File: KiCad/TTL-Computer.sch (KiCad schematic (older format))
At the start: 0 parts

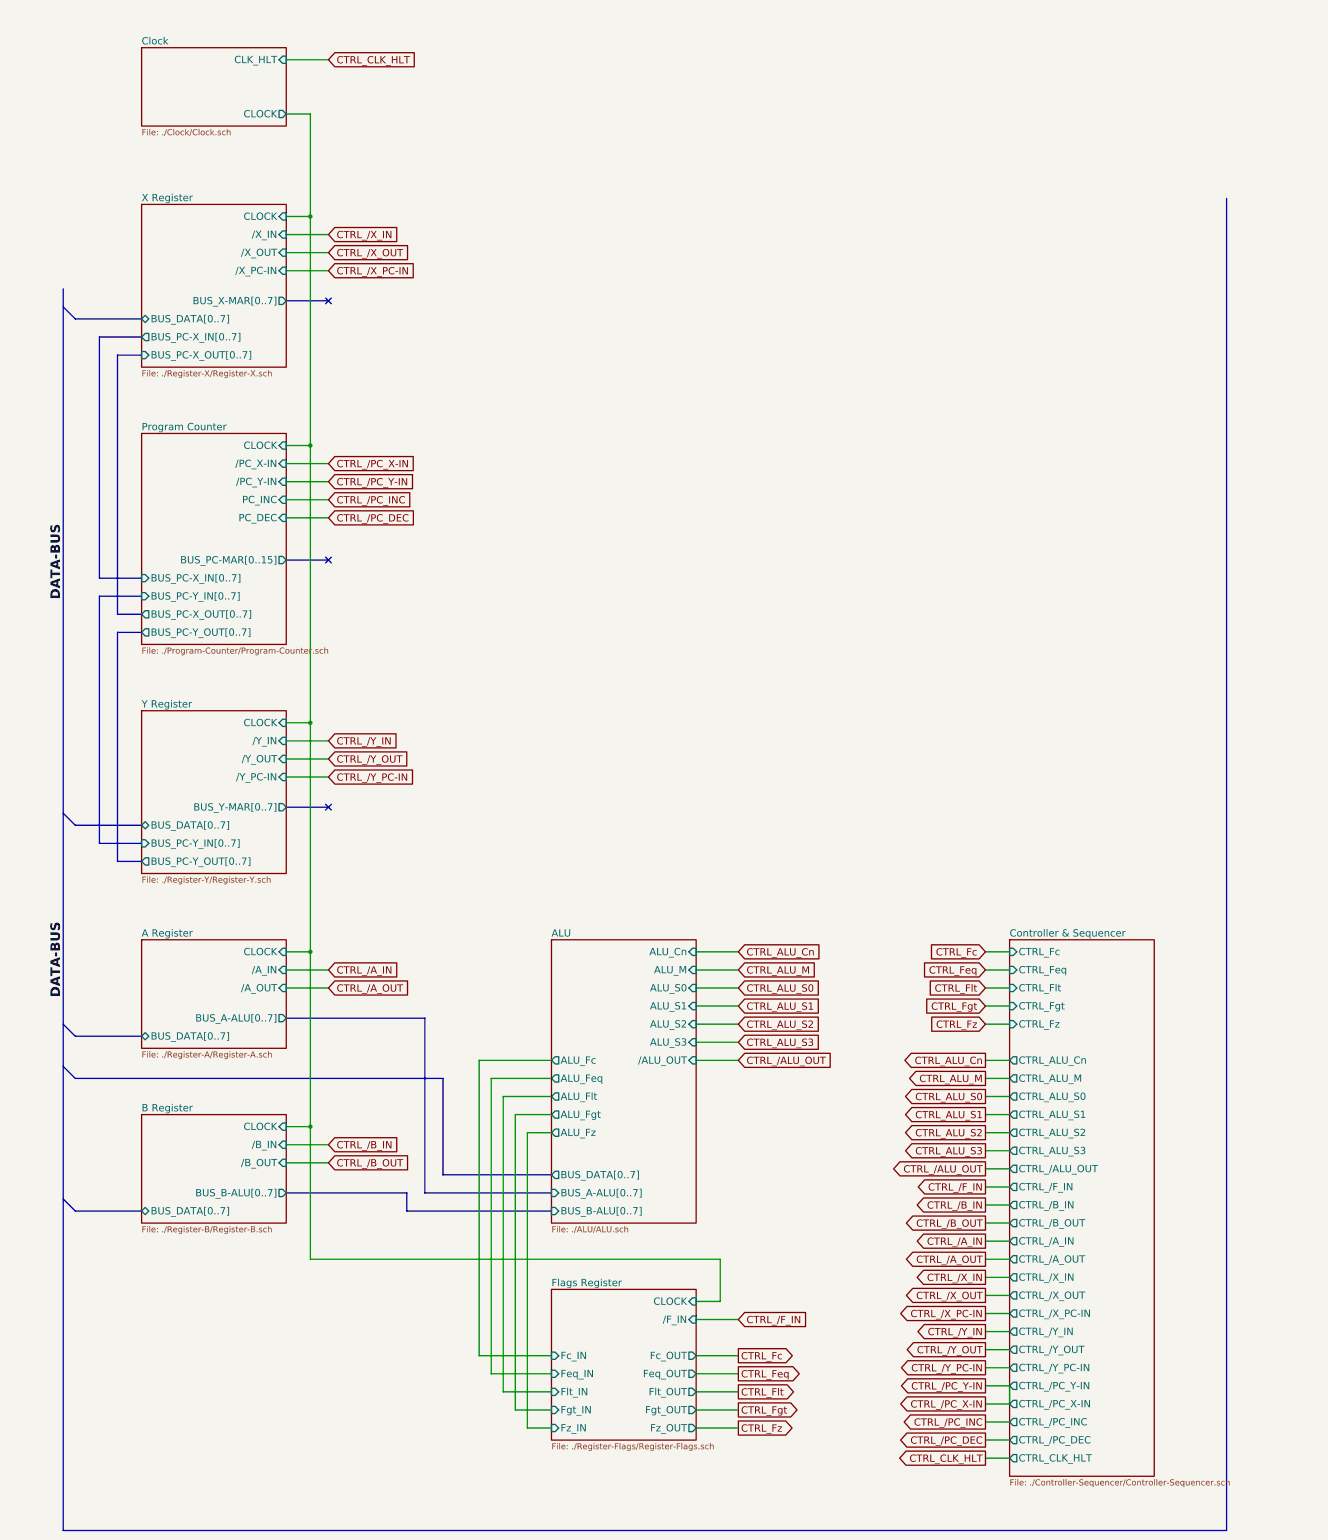
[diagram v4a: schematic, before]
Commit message: Improved ALU and instructions (ALU now takes data from all registers)
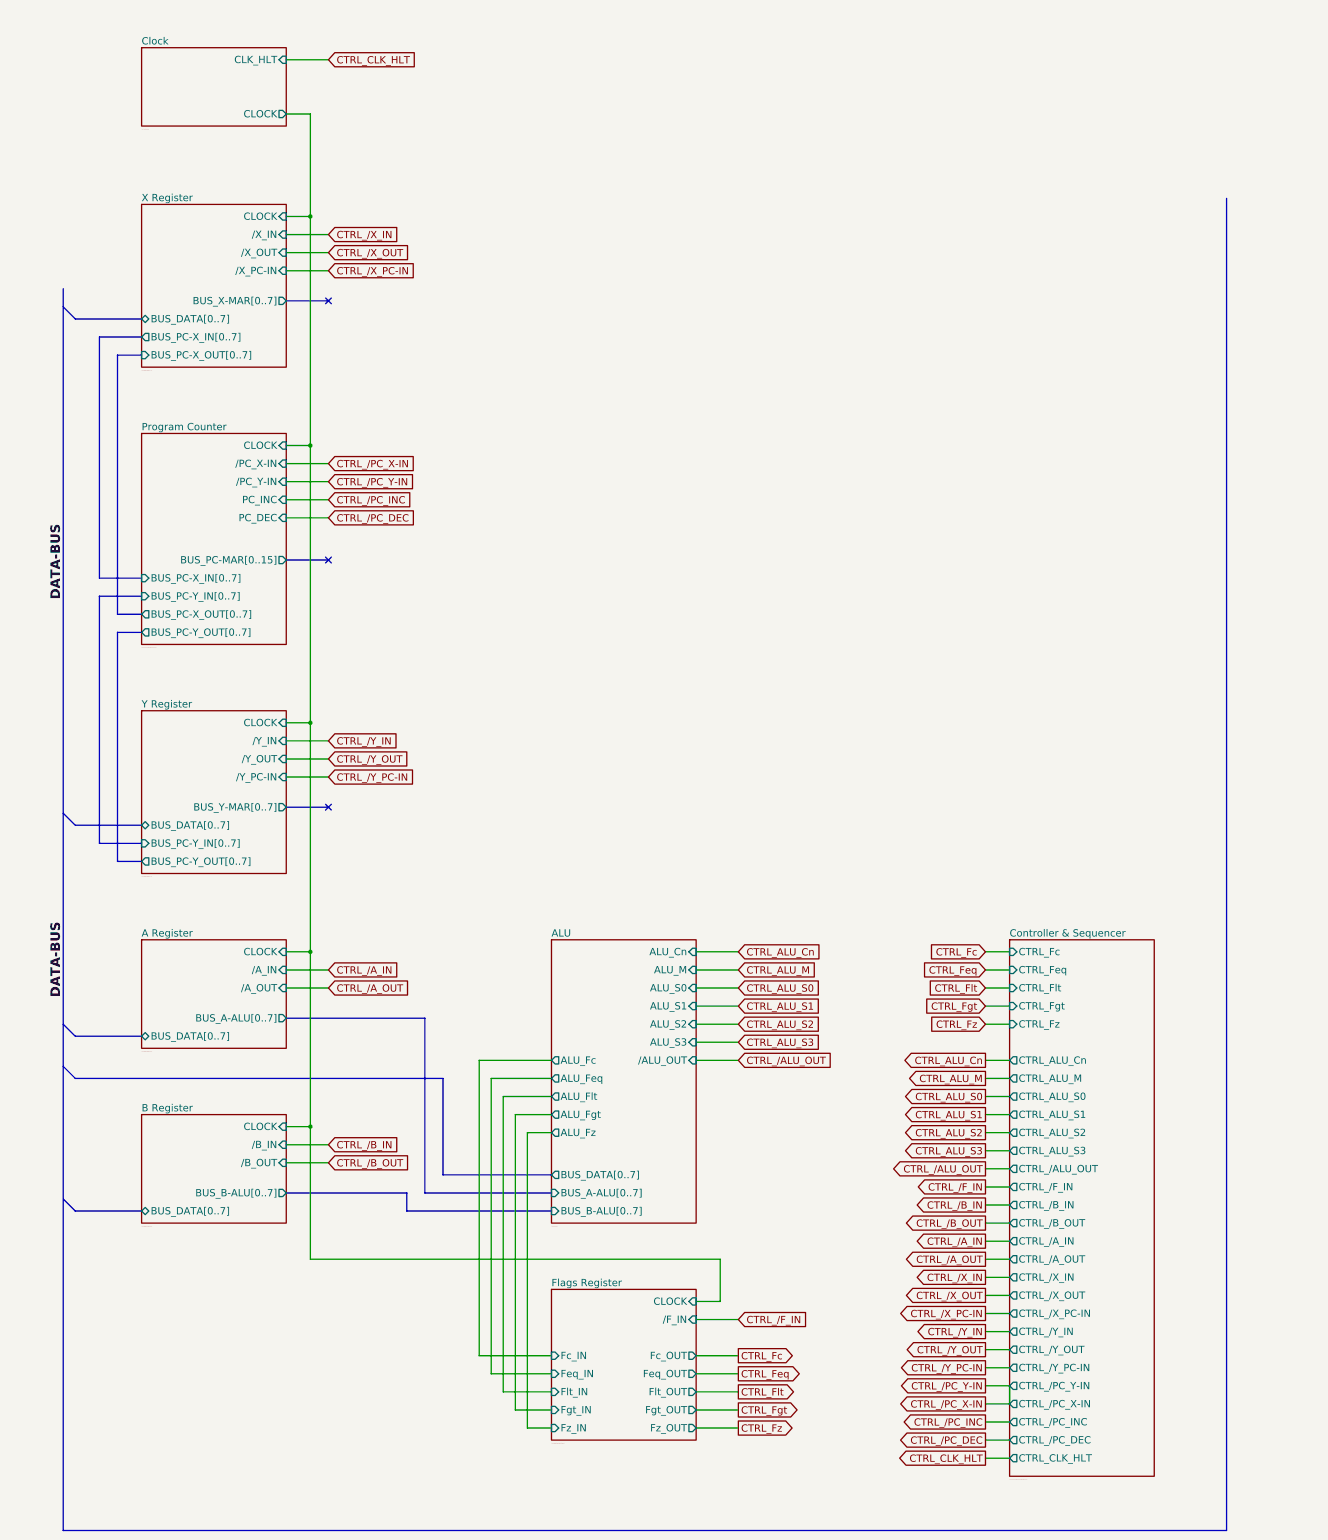
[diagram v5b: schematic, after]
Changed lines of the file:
@@
 U 5ACF3206
 F0 "Clock" 60
-F1 "./Clock/Clock.sch" 0
+F1 "./Clock/Clock.sch" 4
 F2 "CLOCK" O R 2850 1550 60
 F3 "CLK_HLT" I R 2850 1100 60
@@
 U 5ACF2F0F
 F0 "X Register" 60
-F1 "./Register-X/Register-X.sch" 0
+F1 "./Register-X/Register-X.sch" 4
 F2 "CLOCK" I R 2850 2400 60
 F3 "/X_IN" I R 2850 2550 60
@@
 U 5AD0848F
 F0 "Y Register" 60
-F1 "./Register-Y/Register-Y.sch" 0
+F1 "./Register-Y/Register-Y.sch" 4
 F2 "BUS_PC-Y_IN[0..7]" I L 1650 7600 60
 F3 "BUS_DATA[0..7]" B L 1650 7450 60
@@
 U 5ACF340E
 F0 "Program Counter" 60
-F1 "./Program-Counter/Program-Counter.sch" 0
+F1 "./Program-Counter/Program-Counter.sch" 4
 F2 "/PC_X-IN" I R 2850 4450 60
 F3 "/PC_Y-IN" I R 2850 4600 60
@@
 U 5AD5CFF9
 F0 "ALU" 60
-F1 "./ALU/ALU.sch" 0
+F1 "./ALU/ALU.sch" 4
 F2 "ALU_Cn" I R 6250 8500 60
 F3 "ALU_M" I R 6250 8650 60
@@
 U 5AEB52B5
 F0 "B Register" 60
-F1 "./Register-B/Register-B.sch" 0
+F1 "./Register-B/Register-B.sch" 4
 F2 "/B_OUT" I R 2850 10250 60
 F3 "CLOCK" I R 2850 9950 60
@@
 U 5AEB1288
 F0 "A Register" 60
-F1 "./Register-A/Register-A.sch" 0
+F1 "./Register-A/Register-A.sch" 4
 F2 "/A_OUT" I R 2850 8800 60
 F3 "CLOCK" I R 2850 8500 60
@@
 U 5AECAFE0
 F0 "Flags Register" 60
-F1 "./Register-Flags/Register-Flags.sch" 0
+F1 "./Register-Flags/Register-Flags.sch" 4
 F2 "CLOCK" I R 6250 11400 60
 F3 "/F_IN" I R 6250 11550 60
@@
 U 5AF221CC
 F0 "Controller & Sequencer" 60
-F1 "./Controller-Sequencer/Controller-Sequencer.sch" 0
+F1 "./Controller-Sequencer/Controller-Sequencer.sch" 4
 F2 "CTRL_Fc" I L 8850 8500 60
 F3 "CTRL_Feq" I L 8850 8650 60

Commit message: Renamed registers X and Y to C and D.
ALU now has its own internal accumulator register.
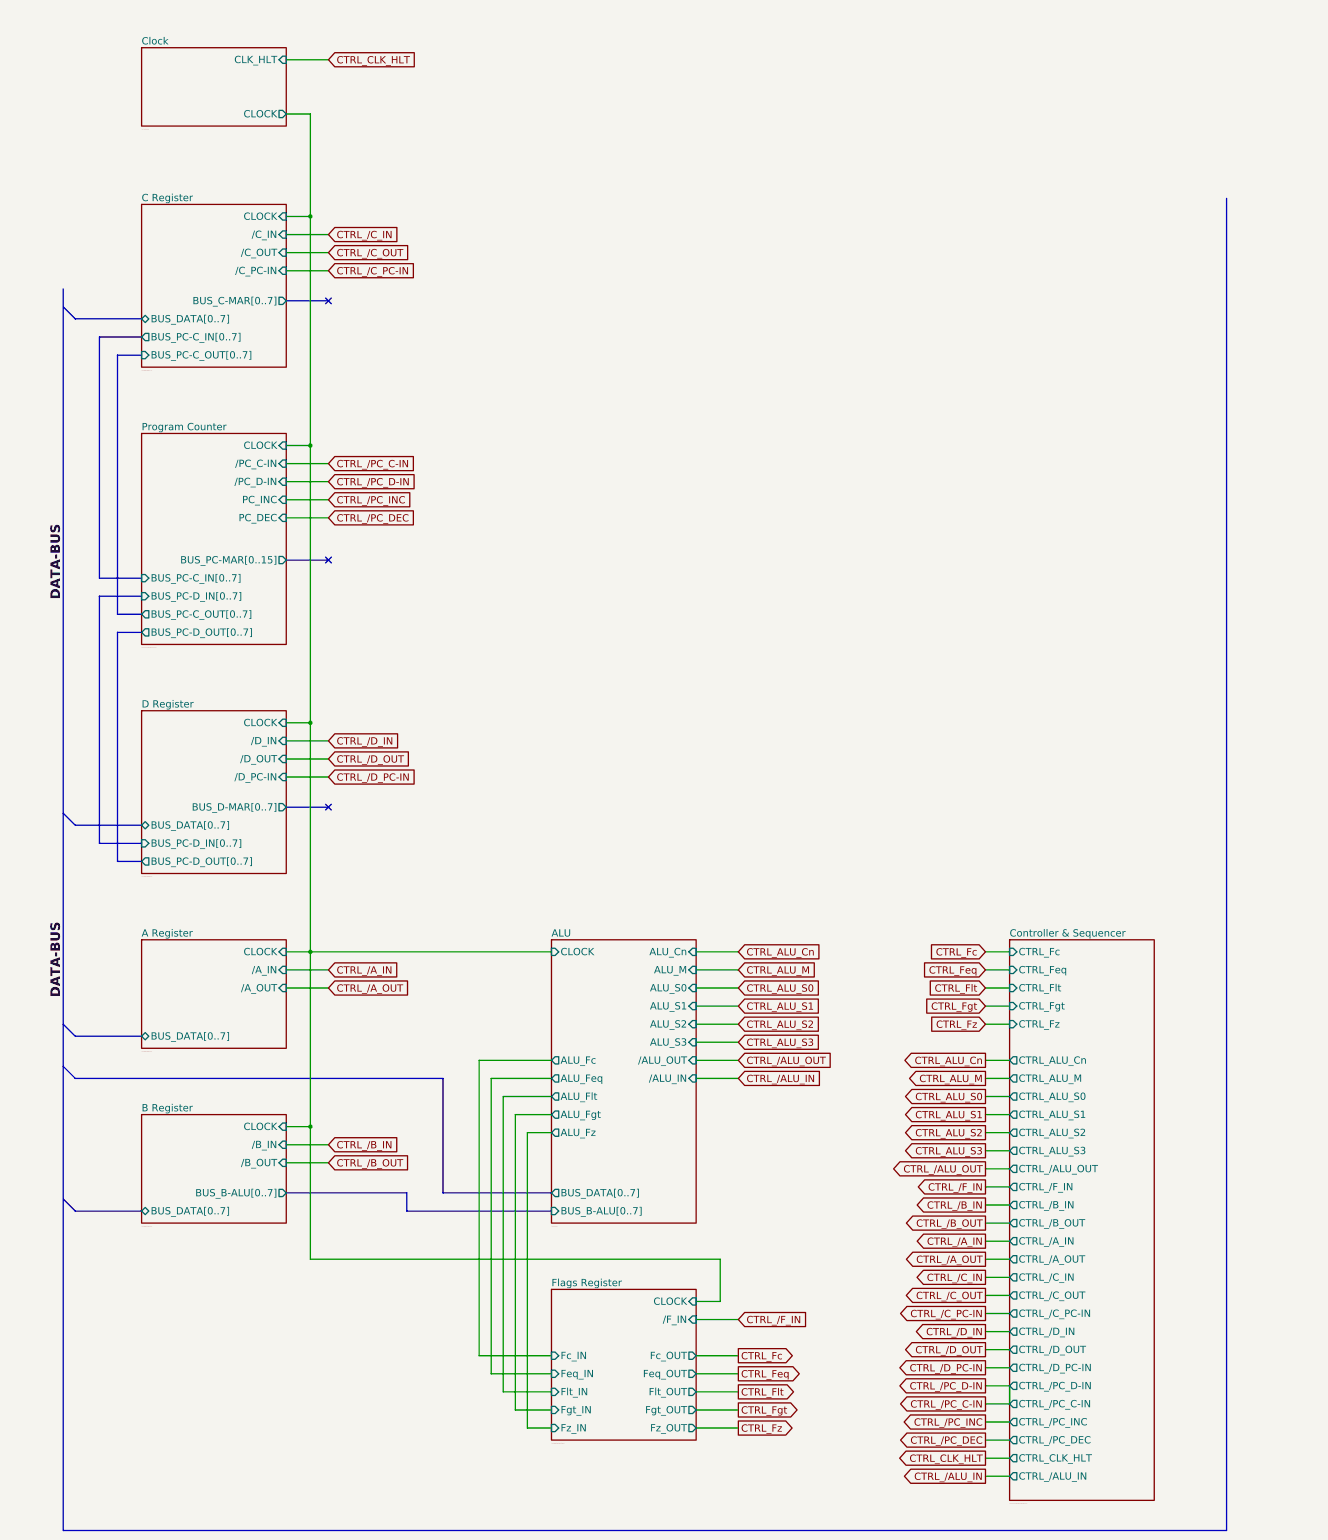
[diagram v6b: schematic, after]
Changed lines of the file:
@@
 S 1650 2300 1200 1350
 U 5ACF2F0F
-F0 "X Register" 60
-F1 "./Register-X/Register-X.sch" 4
+F0 "C Register" 60
+F1 "./Register-C/Register-C.sch" 4
 F2 "CLOCK" I R 2850 2400 60
-F3 "/X_IN" I R 2850 2550 60
-F4 "/X_OUT" I R 2850 2700 60
-F5 "/X_PC-IN" I R 2850 2850 60
+F3 "/C_IN" I R 2850 2550 60
+F4 "/C_OUT" I R 2850 2700 60
+F5 "/C_PC-IN" I R 2850 2850 60
 F6 "BUS_DATA[0..7]" B L 1650 3250 60
-F7 "BUS_PC-X_OUT[0..7]" I L 1650 3550 60
-F8 "BUS_X-MAR[0..7]" O R 2850 3100 60
-F9 "BUS_PC-X_IN[0..7]" O L 1650 3400 60
+F7 "BUS_PC-C_OUT[0..7]" I L 1650 3550 60
+F8 "BUS_C-MAR[0..7]" O R 2850 3100 60
+F9 "BUS_PC-C_IN[0..7]" O L 1650 3400 60
 $EndSheet
 $Sheet
 S 1650 6500 1200 1350
 U 5AD0848F
-F0 "Y Register" 60
-F1 "./Register-Y/Register-Y.sch" 4
-F2 "BUS_PC-Y_IN[0..7]" I L 1650 7600 60
+F0 "D Register" 60
+F1 "./Register-D/Register-D.sch" 4
+F2 "BUS_PC-D_IN[0..7]" I L 1650 7600 60
 F3 "BUS_DATA[0..7]" B L 1650 7450 60
 F4 "CLOCK" I R 2850 6600 60
-F5 "BUS_Y-MAR[0..7]" O R 2850 7300 60
-F6 "/Y_IN" I R 2850 6750 60
-F7 "/Y_OUT" I R 2850 6900 60
-F8 "/Y_PC-IN" I R 2850 7050 60
-F9 "BUS_PC-Y_OUT[0..7]" O L 1650 7750 60
+F5 "BUS_D-MAR[0..7]" O R 2850 7300 60
+F6 "/D_IN" I R 2850 6750 60
+F7 "/D_OUT" I R 2850 6900 60
+F8 "/D_PC-IN" I R 2850 7050 60
+F9 "BUS_PC-D_OUT[0..7]" O L 1650 7750 60
 $EndSheet
 $Sheet
@@
 F0 "Program Counter" 60
 F1 "./Program-Counter/Program-Counter.sch" 4
-F2 "/PC_X-IN" I R 2850 4450 60
-F3 "/PC_Y-IN" I R 2850 4600 60
+F2 "/PC_C-IN" I R 2850 4450 60
+F3 "/PC_D-IN" I R 2850 4600 60
 F4 "PC_INC" I R 2850 4750 60
 F5 "PC_DEC" I R 2850 4900 60
 F6 "CLOCK" I R 2850 4300 60
-F7 "BUS_PC-X_OUT[0..7]" O L 1650 5700 60
-F8 "BUS_PC-Y_OUT[0..7]" O L 1650 5850 60
+F7 "BUS_PC-C_OUT[0..7]" O L 1650 5700 60
+F8 "BUS_PC-D_OUT[0..7]" O L 1650 5850 60
 F9 "BUS_PC-MAR[0..15]" O R 2850 5250 60
-F10 "BUS_PC-X_IN[0..7]" I L 1650 5400 60
-F11 "BUS_PC-Y_IN[0..7]" I L 1650 5550 60
+F10 "BUS_PC-C_IN[0..7]" I L 1650 5400 60
+F11 "BUS_PC-D_IN[0..7]" I L 1650 5550 60
 $EndSheet
 $Sheet
@@
 F2 "ALU_Cn" I R 6250 8500 60
 F3 "ALU_M" I R 6250 8650 60
-F4 "BUS_A-ALU[0..7]" I L 5050 10500 60
-F5 "BUS_B-ALU[0..7]" I L 5050 10650 60
-F6 "ALU_S0" I R 6250 8800 60
-F7 "ALU_S1" I R 6250 8950 60
-F8 "ALU_S2" I R 6250 9100 60
-F9 "ALU_S3" I R 6250 9250 60
-F10 "ALU_Feq" O L 5050 9550 60
-F11 "ALU_Flt" O L 5050 9700 60
-F12 "ALU_Fgt" O L 5050 9850 60
-F13 "/ALU_OUT" I R 6250 9400 60
-F14 "BUS_DATA[0..7]" O L 5050 10350 60
-F15 "ALU_Fz" O L 5050 10000 60
-F16 "ALU_Fc" O L 5050 9400 60
+F4 "BUS_B-ALU[0..7]" I L 5050 10650 60
+F5 "ALU_S0" I R 6250 8800 60
+F6 "ALU_S1" I R 6250 8950 60
+F7 "ALU_S2" I R 6250 9100 60
+F8 "ALU_S3" I R 6250 9250 60
+F9 "ALU_Feq" O L 5050 9550 60
+F10 "ALU_Flt" O L 5050 9700 60
+F11 "ALU_Fgt" O L 5050 9850 60
+F12 "/ALU_OUT" I R 6250 9400 60
+F13 "BUS_DATA[0..7]" O L 5050 10500 60
+F14 "ALU_Fz" O L 5050 10000 60
+F15 "ALU_Fc" O L 5050 9400 60
+F16 "CLOCK" I L 5050 8500 60
+F17 "/ALU_IN" I R 6250 9550 60
 $EndSheet
 Entry Bus Bus
@@
 F3 "CLOCK" I R 2850 8500 60
 F4 "BUS_DATA[0..7]" B L 1650 9200 60
-F5 "BUS_A-ALU[0..7]" O R 2850 9050 60
-F6 "/A_IN" I R 2850 8650 60
+F5 "/A_IN" I R 2850 8650 60
 $EndSheet
 Entry Bus Bus
@@
 $EndSheet
 Text GLabel 3200 2550 2    60   Input ~ 0
-CTRL_/X_IN
+CTRL_/C_IN
 Text GLabel 3200 2700 2    60   Input ~ 0
-CTRL_/X_OUT
+CTRL_/C_OUT
 Text GLabel 3200 2850 2    60   Input ~ 0
-CTRL_/X_PC-IN
+CTRL_/C_PC-IN
 Text GLabel 3200 4450 2    60   Input ~ 0
-CTRL_/PC_X-IN
+CTRL_/PC_C-IN
 Text GLabel 3200 4600 2    60   Input ~ 0
-CTRL_/PC_Y-IN
+CTRL_/PC_D-IN
 Text GLabel 3200 4750 2    60   Input ~ 0
 CTRL_/PC_INC
@@
 NoConn ~ 3200 5250
 Text GLabel 3200 6750 2    60   Input ~ 0
-CTRL_/Y_IN
+CTRL_/D_IN
 Text GLabel 3200 6900 2    60   Input ~ 0
-CTRL_/Y_OUT
+CTRL_/D_OUT
 Text GLabel 3200 7050 2    60   Input ~ 0
-CTRL_/Y_PC-IN
+CTRL_/D_PC-IN
 NoConn ~ 3200 7300
 Text GLabel 3200 8650 2    60   Input ~ 0
@@
 CTRL_/PC_INC
 Text GLabel 8650 12250 0    60   Output ~ 0
-CTRL_/PC_X-IN
+CTRL_/PC_C-IN
 Text GLabel 8650 12100 0    60   Output ~ 0
-CTRL_/PC_Y-IN
+CTRL_/PC_D-IN
 Text GLabel 8650 11950 0    60   Output ~ 0
-CTRL_/Y_PC-IN
+CTRL_/D_PC-IN
 Text GLabel 8650 11800 0    60   Output ~ 0
-CTRL_/Y_OUT
+CTRL_/D_OUT
 Text GLabel 8650 11650 0    60   Output ~ 0
-CTRL_/Y_IN
+CTRL_/D_IN
 Text GLabel 8650 11500 0    60   Output ~ 0
-CTRL_/X_PC-IN
+CTRL_/C_PC-IN
 Text GLabel 8650 11350 0    60   Output ~ 0
-CTRL_/X_OUT
+CTRL_/C_OUT
 Text GLabel 8650 11200 0    60   Output ~ 0
-CTRL_/X_IN
+CTRL_/C_IN
 Text GLabel 8650 11050 0    60   Output ~ 0
 CTRL_/A_OUT
@@
 	1100 10650 1650 10650
 Wire Wire Line
-	3050 8500 2850 8500
+	2850 8500 5050 8500
 Connection ~ 3050 6600
 Wire Wire Line
@@
 	3850 10650 5050 10650
 Wire Bus Line
-	2850 9050 4000 9050
-Wire Bus Line
-	4000 9050 4000 10500
-Wire Bus Line
-	4000 10500 5050 10500
-Wire Bus Line
 	1100 9550 4150 9550
 Wire Bus Line
-	4150 9550 4150 10350
-Wire Bus Line
-	4150 10350 5050 10350
+	4150 9550 4150 10500
+Wire Bus Line
+	4150 10500 5050 10500
 Wire Wire Line
 	5050 10000 4850 10000
@@
 	8650 8500 8850 8500
 $Sheet
-S 8850 8400 1200 4450
+S 8850 8400 1200 4650
 U 5AF221CC
 F0 "Controller & Sequencer" 60
@@
 F17 "CTRL_/A_IN" O L 8850 10900 60
 F18 "CTRL_/A_OUT" O L 8850 11050 60
-F19 "CTRL_/X_IN" O L 8850 11200 60
-F20 "CTRL_/X_OUT" O L 8850 11350 60
-F21 "CTRL_/X_PC-IN" O L 8850 11500 60
-F22 "CTRL_/Y_IN" O L 8850 11650 60
-F23 "CTRL_/Y_OUT" O L 8850 11800 60
-F24 "CTRL_/Y_PC-IN" O L 8850 11950 60
-F25 "CTRL_/PC_Y-IN" O L 8850 12100 60
-F26 "CTRL_/PC_X-IN" O L 8850 12250 60
+F19 "CTRL_/C_IN" O L 8850 11200 60
+F20 "CTRL_/C_OUT" O L 8850 11350 60
+F21 "CTRL_/C_PC-IN" O L 8850 11500 60
+F22 "CTRL_/D_IN" O L 8850 11650 60
+F23 "CTRL_/D_OUT" O L 8850 11800 60
+F24 "CTRL_/D_PC-IN" O L 8850 11950 60
+F25 "CTRL_/PC_D-IN" O L 8850 12100 60
+F26 "CTRL_/PC_C-IN" O L 8850 12250 60
 F27 "CTRL_/PC_INC" O L 8850 12400 60
 F28 "CTRL_/PC_DEC" O L 8850 12550 60
 F29 "CTRL_CLK_HLT" O L 8850 12700 60
-$EndSheet
+F30 "CTRL_/ALU_IN" O L 8850 12850 60
+$EndSheet
+Text GLabel 8650 12850 0    60   Output ~ 0
+CTRL_/ALU_IN
+Wire Wire Line
+	8650 12850 8850 12850
+Text GLabel 6600 9550 2    60   Input ~ 0
+CTRL_/ALU_IN
+Wire Wire Line
+	6600 9550 6250 9550
 $EndSCHEMATC
